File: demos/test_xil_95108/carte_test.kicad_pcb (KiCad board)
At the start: 2 copper layers, 42 parts, among them J1 DB25, J2 DB9FEM, K1 CONN_3, P2 CONN_3, P3 CONN_2, P4 CONN_2X2, SW1 SW_PUSH, SW2 SW_PUSH, U1 TDA8702, U2 XC95108PC84, U3 LM7805, U4 74HC04, U5 RAM_32KO, U6 LM318N, X1 10MHz

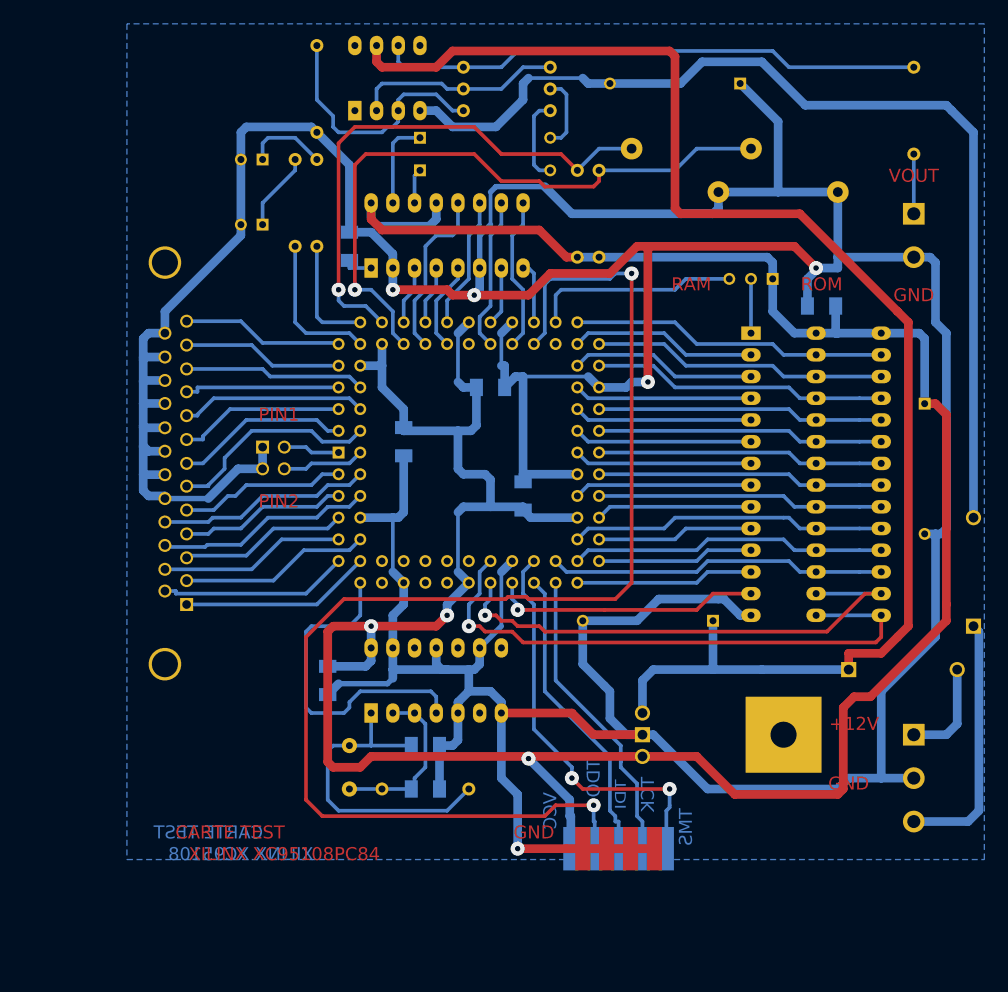
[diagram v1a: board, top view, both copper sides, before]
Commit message: Update demo files. A minor code cleaning.
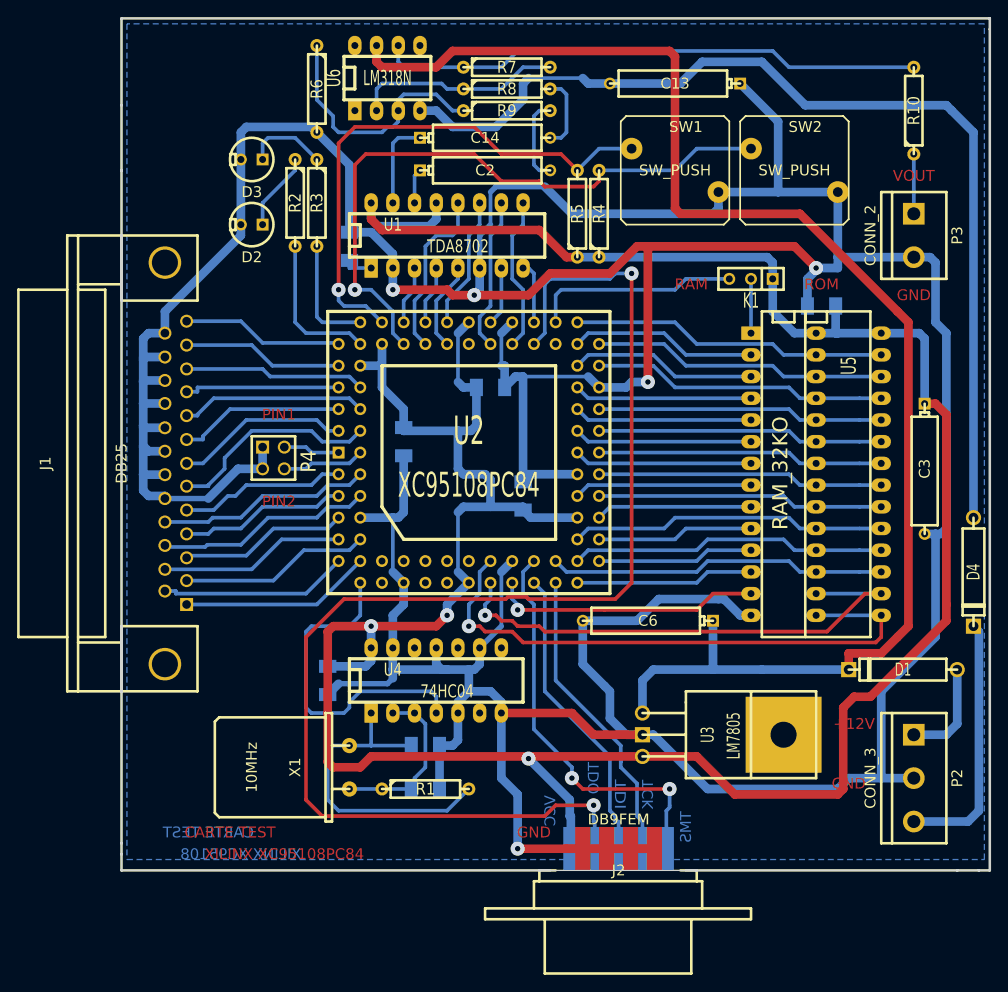
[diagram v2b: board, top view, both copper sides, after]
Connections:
- net CSMEM_1 renamed /CSMEM
- net DAT0_1 renamed /DAT0
- net DAT1_1 renamed /DAT1
- net DAT2_1 renamed /DAT2
- net DAT3_1 renamed /DAT3
- net DAT4_1 renamed /DAT4
- net DAT5_1 renamed /DAT5
- net DAT6_1 renamed /DAT6
- net DAT7_1 renamed /DAT7
- net DCLK_1 renamed /DCLK
- net LED1_1 renamed /LED1
- net LED2_1 renamed /LED2
- net MA0_1 renamed /MA0
- net MA1_1 renamed /MA1
- net MA2_1 renamed /MA2
- net MA3_1 renamed /MA3
- net MA4_1 renamed /MA4
- net MA5_1 renamed /MA5
- net MA6_1 renamed /MA6
- net MA7_1 renamed /MA7
- net MD0_1 renamed /MD0
- net MD10_1 renamed /MD10
- net MD11_1 renamed /MD11
- net MD12_1 renamed /MD12
- net MD13_1 renamed /MD13
- net MD14_1 renamed /MD14
- net MD1_1 renamed /MD1
- net MD2_1 renamed /MD2
- net MD3_1 renamed /MD3
- net MD4_1 renamed /MD4
- net MD5_1 renamed /MD5
- net MD6_1 renamed /MD6
- net MD7_1 renamed /MD7
- net MD8_1 renamed /MD8
- net MD9_1 renamed /MD9
- net OEMEM_1 renamed /OEMEM
- net PARBUS0_1 renamed /PARBUS0
- net PARBUS1_1 renamed /PARBUS1
- net PARBUS2_1 renamed /PARBUS2
- net PARBUS3_1 renamed /PARBUS3
- net PARBUS4_1 renamed /PARBUS4
- net PARBUS5_1 renamed /PARBUS5
- net PARBUS6_1 renamed /PARBUS6
- net PARBUS7_1 renamed /PARBUS7
- net PAR_AUX0_X00001 renamed /PAR_AUX0/STROBE*
- net PAR_AUX1_X00004 renamed /PAR_AUX1/ERROR*
- net PAR_AUX2_X00003 renamed /PAR_AUX2/AUTOLF*
- net PAR_AUX3_X00002 renamed /PAR_AUX3/SELECT*
- net PAR_AUX4/PE_1 renamed /PAR_AUX4/PE
- net PAR_AUX5/BUSY*_1 renamed /PAR_AUX5/BUSY*
- net PAR_AUX6/ACK_1 renamed /PAR_AUX6/ACK
- net PAR_AUX7/INIT_1 renamed /PAR_AUX7/INIT
- net PAR_AUX8_X00005 renamed /PAR_AUX8/SELECT
- net PIN_TEST0_1 renamed /PIN_TEST0
- net PIN_TEST1_1 renamed /PIN_TEST1
- net R/W-A14_1 renamed /R/W-A14
- net SW0_1 renamed /SW0
- net SW1_1 renamed /SW1
- net TCK_1 renamed /TCK
- net TDI_1 renamed /TDI
- net TDO_1 renamed /TDO
- net TMS_1 renamed /TMS
- net XIN/CLK_1 renamed /XIN/CLK
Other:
- board outline added: 101.6 x 99.7 mm

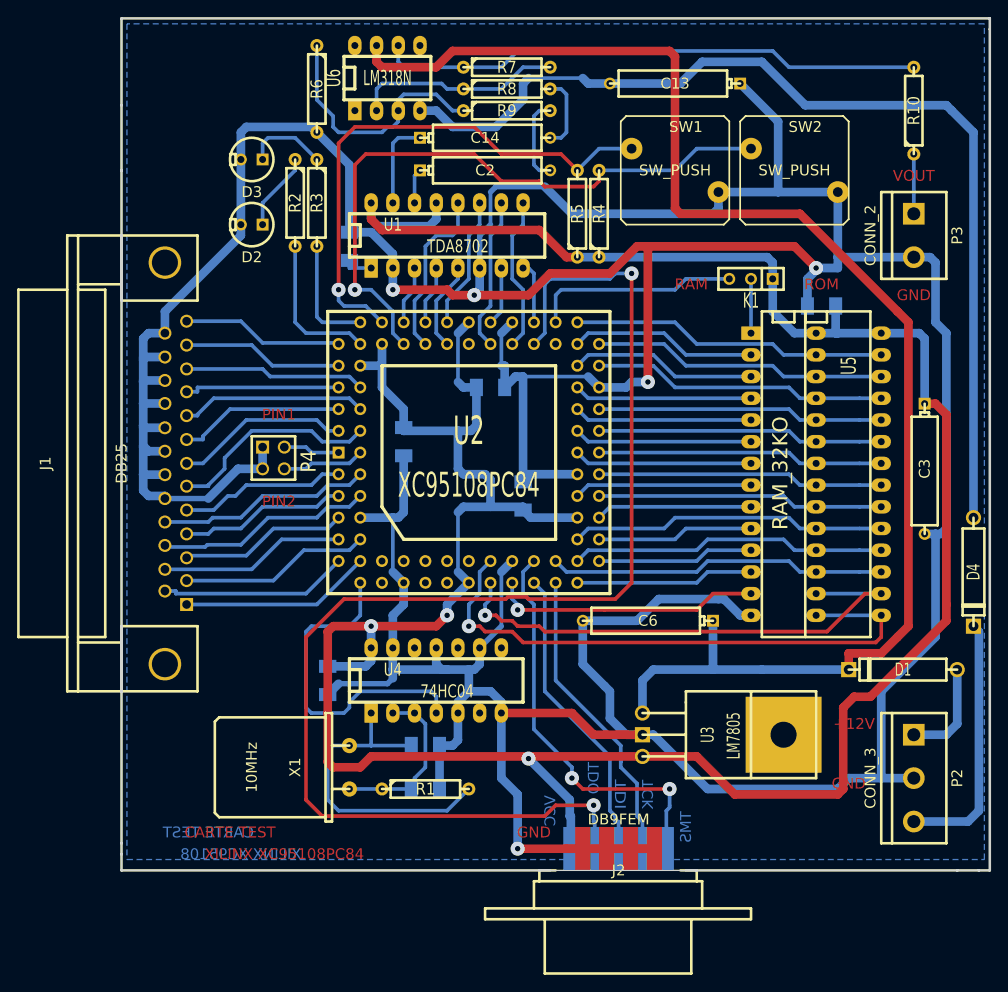
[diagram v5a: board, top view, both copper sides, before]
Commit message: Footprint wizard: fixes and enhancements in python scripts.
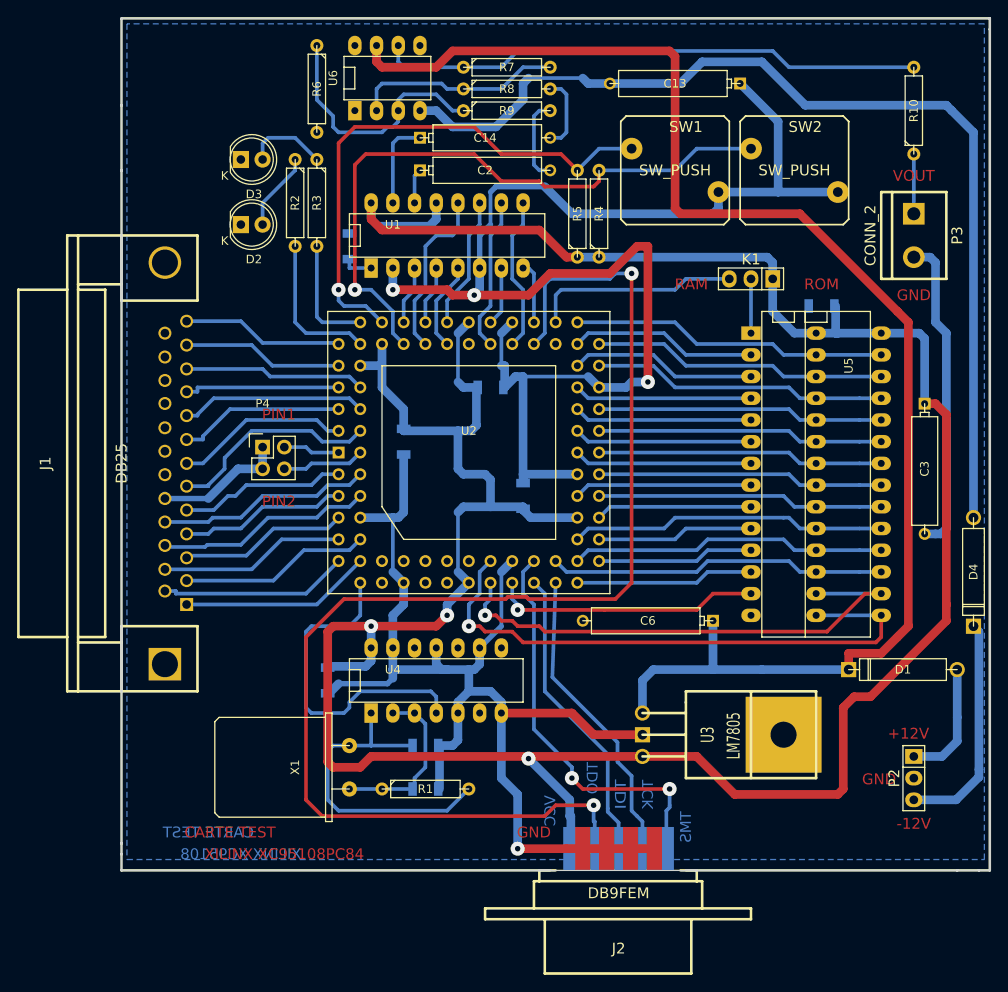
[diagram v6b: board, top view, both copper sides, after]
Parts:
- C1, C10, C11, C12, C4, C5, C7, C8: footprint SM1206 -> Capacitors_SMD:C_1206
- C13, C14, C2, C3, C6: footprint CP6 -> Discret:CP6
- D1, D4: footprint D5 -> Discret:D5
- D2, D3: footprint LEDV -> LEDs:LED-5MM
- J1: footprint DB25FC -> Connect:DB25FC
- J2: footprint DB9F_CI_INVERT -> Connect:DB9F_CI_INVERT
- K1: footprint SIL-3 -> Socket_Strips:Socket_Strip_Straight_1x03
- P2: footprint bornier3 -> Socket_Strips:Socket_Strip_Straight_1x03
- P3: footprint bornier2 -> Connect:bornier2
- P4: footprint head_2x2 -> Pin_Headers:Pin_Header_Straight_2x02
- R1, R10, R2, R3, R4, R5, R6, R7, R8, R9: footprint R4 -> Discret:R4
- SW1, SW2: footprint SW_PUSH -> Discret:SW_PUSH
- U1: footprint 16DIP-ELL300 -> Sockets_DIP:DIP-16__300_ELL
- U2: footprint PLCC84 -> Sockets:PLCC84
- U3: footprint LM78XX -> Discret:LM78XX
- U4: footprint 14DIP-ELL300 -> Sockets_DIP:DIP-14__300_ELL
- U5: footprint 28DIP-ELL300-600 -> Sockets_DIP:DIP-28__300__600_ELL
- U6: footprint 8DIP-ELL300 -> Sockets_DIP:DIP-8__300_ELL
- X1: footprint HC-18UH -> Crystals:HC-18UH
- moved P4 1.80 mm to (111.1, 86.4), turned to 0 degrees
- moved D2 1.27 mm to (108.6, 60.3), turned to 0 degrees
- moved D3 1.27 mm to (108.6, 52.7), turned to 0 degrees
- turned K1 to 0 degrees
- turned P2 to 90 degrees
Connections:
- D1 pad 1: Net-(D1-Pad1) -> +12V
- D1 pad 2: +12V -> /+12BATT
- D2 pad 1: Net-(D2-Pad1) -> GND
- D2 pad 2: GND -> Net-(D2-Pad2)
- D3 pad 1: Net-(D3-Pad1) -> GND
- D3 pad 2: GND -> Net-(D3-Pad2)
- D4 pad 1: -12V -> /-12BATT
- D4 pad 2: Net-(D4-Pad2) -> -12V
- P2 pad 1: Net-(D1-Pad1) -> /+12BATT
- P2 pad 3: Net-(D4-Pad2) -> /-12BATT
- R2 pad 1: Net-(D2-Pad1) -> Net-(D2-Pad2)
- R3 pad 1: Net-(D3-Pad1) -> Net-(D3-Pad2)
- U2 pad 14: (no net) -> Net-(U2-Pad14)
- U2 pad 15: (no net) -> Net-(U2-Pad15)
- U2 pad 17: (no net) -> Net-(U2-Pad17)
- U2 pad 18: (no net) -> Net-(U2-Pad18)
- U2 pad 19: (no net) -> Net-(U2-Pad19)
- U2 pad 20: (no net) -> Net-(U2-Pad20)
- U2 pad 21: (no net) -> Net-(U2-Pad21)
- U2 pad 23: (no net) -> Net-(U2-Pad23)
- U2 pad 57: (no net) -> Net-(U2-Pad57)
- U2 pad 65: (no net) -> Net-(U2-Pad65)
- U4 pad 10: (no net) -> Net-(U4-Pad10)
- U4 pad 12: (no net) -> Net-(U4-Pad12)
- U4 pad 6: (no net) -> Net-(U4-Pad6)
- U4 pad 8: (no net) -> Net-(U4-Pad8)
- U6 pad 1: (no net) -> Net-(U6-Pad1)
- U6 pad 5: (no net) -> Net-(U6-Pad5)
- U6 pad 8: (no net) -> Net-(U6-Pad8)
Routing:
- net GND: track 619.6 -> 361.0 mm, vias 5 -> 4
- net Net-(D4-Pad2): track 30.0 -> 0.00 mm
- net /-12BATT: track 0.00 -> 26.6 mm
- net /+12BATT: track 0.00 -> 14.2 mm
- net Net-(D1-Pad1): track 12.0 -> 0.00 mm
- net Net-(D3-Pad2): track 0.00 -> 9.57 mm
- net Net-(D3-Pad1): track 9.57 -> 0.00 mm
- net Net-(D2-Pad2): track 0.00 -> 9.20 mm
- net Net-(D2-Pad1): track 9.20 -> 0.00 mm
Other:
- board text added: "-12V"
